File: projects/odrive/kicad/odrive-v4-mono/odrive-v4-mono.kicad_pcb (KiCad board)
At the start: 4 copper layers, 140 x 112 mm, 325 parts, among them J1 PC 16/2-ST, J10 ENC_M1_JST-GH, J11 ENC_SPI_JST-GH, J12 GPIO_2x4, J13 BRAKE_EXT, J2 M0 A/B/C, J4 FTSH-105-01-L-DV-K, J5 FAN 12V 150mA MAX, J6 USB4105-GF-A, J7 JST-GH-4 CAN, J8 JST-GH-4 CAN, J9 ENC_M0_JST-GH, Q1 NVMFS5C628NL | BSC027N10NS5, Q10 NVMFS5C628NL, Q11 NVMFS5C628NL, Q12 NVMFS5C628NL, Q13 NVMFS5C628NL, Q14 NVMFS5C628NL, Q15 NVMFS5C628NL, Q16 NVMFS5C628NL, Q17 NVMFS5C628NL, Q18 NVMFS5C628NL, Q19 NVMFS5C628NL, Q20 NVMFS5C628NL, Q21 NVMFS5C628NL, Q50 NVMFS5C628NL/BSC027N10NS5, Q51 NVMFS5C628NL/BSC027N10NS5, SW1 CAN_TERM, U10 TLV9062, U11 TMUX1204, U12 TLV7031, U13 TLV431, U14 74LVC1G04, U15 74LVC1G08, U16 TPD4E05U06, U2 STM32F405RGT6, U20 LM5164DDA, U21 LMR51430, U22 TLV75533PDBV, U23 TPS7A2033DBV, U25 74LVC1G06, U26 TLV7031DBV, U27 74LVC1G08, U28 TPS3840DL30, U3 DRV8353RS, U30 TPS2553DBV, U31 TPS2553DBV, U32 TPS2553DBV, U33 USBLC6-2SC6, U34 TCAN1042HGV, U35 SN74LVC2G17, U36 SN74LVC2G17, U37 SN74LVC2G17, U38 TPD4E05U06, U39 TPD4E05U06, U40 SN74LVC1G125, U41 TPD4E05U06, U42 TPD1E10B06, U50 UCC27517A, U51 INA181A2, U52 TLV7031, U53 74LVC1G74, U54 74LVC1G32, U55 74LVC1G08, Y1 8MHz

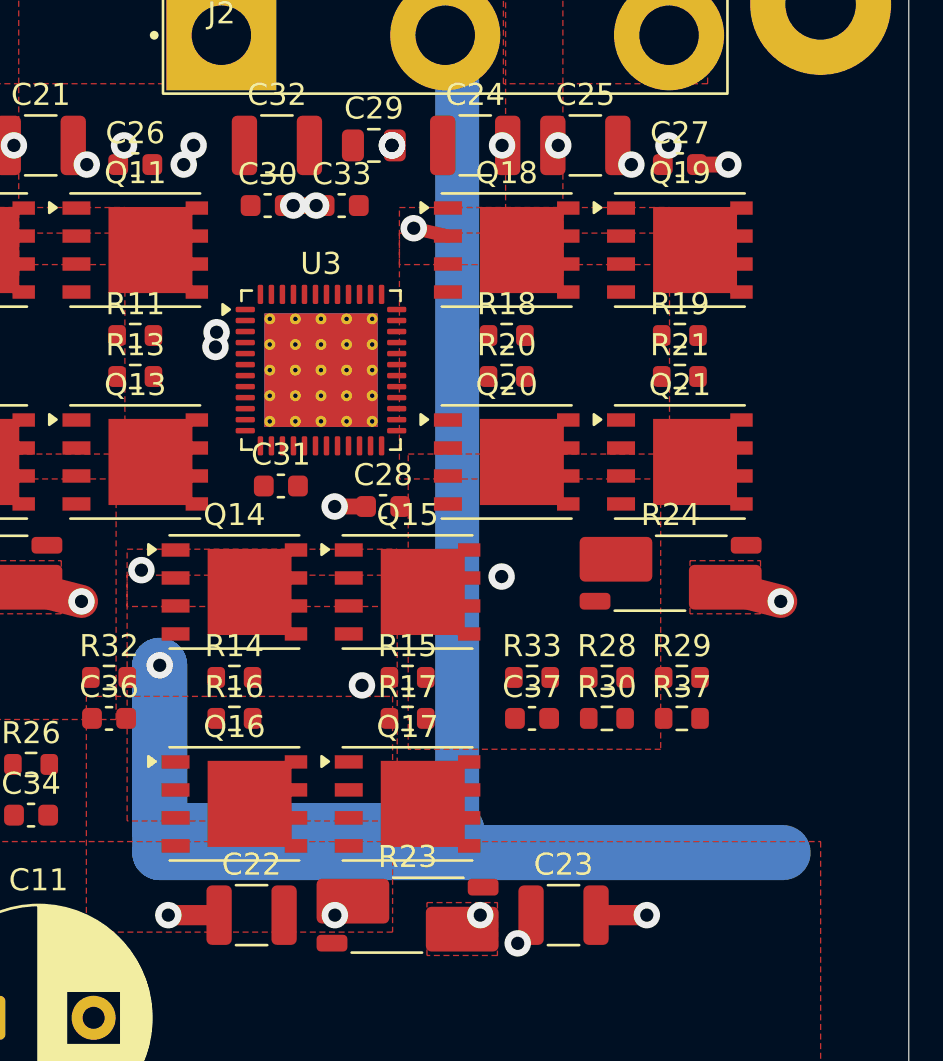
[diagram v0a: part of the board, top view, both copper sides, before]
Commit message: Phase 0 closed: power frozen - 79 items locked, DRC zero, evaluator floors met
The lock is the load-bearing step: ImportSpecctraSES deletes every
unlocked track and via board-wide, so nothing autorouted can be imported
until the power copper is untouchable. All 78 tracks/vias locked via the
SWIG script from the strategy (verified working on 10.0.4), plus the
re-created second M0_B corridor via, 79 total, every one carrying
'(locked yes)' in the file.

Cleanup en route: the dangling leftovers found by the warning-level DRC
sweep - one 28mm orphan segment and a stray SRC_B via from the old B
corridor, plus the mystery M0_CPL via, which turned out to be my own
bug: an earlier via-clone found no '(at 156.0 84.0)' match because KiCad
normalizes '156.0' to '156' on save, and the fallback rfind cloned the
last via in the file instead - a silent exact-duplicate. Coordinate
patterns against a saved board must use the normalized form.

Rule areas are formally skipped, documented in the strategy: KiCad
keepouts cannot exempt existing items and the power columns are full of
our own stitch copper. Locks + layer confinement + G3/G4 gates carry
that protection instead.

Gate results: kicad-cli DRC 0 errors; power_eval via floors all met
(DCBUS 23, PGND 22, M0_B 2); the 43 remaining power unconnected are the
known thin-trace pile (driver pins, bootstrap, snubber taps, brake tail)
owned by the Phase-1 escape pass. Next: escape pre-pass for U2/U3,
route_eval.py, then the freerouting-vs-KRT tournament.
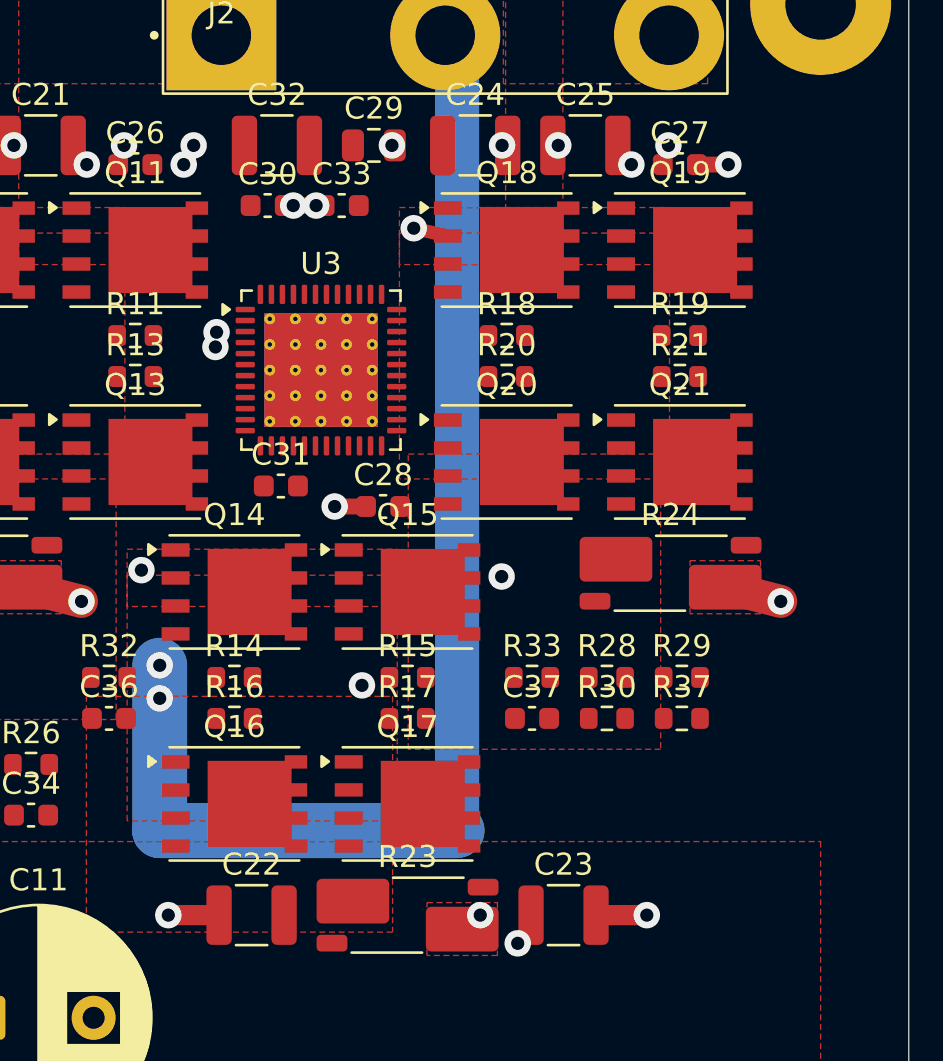
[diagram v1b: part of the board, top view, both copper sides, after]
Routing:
- net /MotorCell M0/M0_B: track 94.0 -> 57.2 mm, vias 1 -> 2
- net /MotorCell M0/M0_SRC_B: vias 1 -> 0
- net /MotorCell M0/M0_CPL: vias 2 -> 1

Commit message: Phase 1: escape pre-pass for the two pin funnels - 87 stubs, DRC zero
The board's routing difficulty concentrates at U2 (LQFP-64, 55 signal
pins) and U3 (QFN-48, 42): inter-pin capacity at 0.5mm pitch with our
rules is exactly zero, so every pin must be walked out of the pad field
before any global routing. This pass does it deterministically.

v1 (radial fan from package centre) taught the lesson: corner pins'
diagonal exits cut toward neighbouring pads - 70 clearance violations at
0.13-0.19mm - because a TRACK has no Reference and the intra-footprint
DRU rule cannot bless it; and the circle approximation of elongated QFN
pads in the self-checker rejected all 97 pins first (the pad's long axis
points ALONG the stub; the lateral half-width is the short dim).

v2: perpendicular exit from each package side, lane-centred by
construction (0.225mm to each neighbour pad against the 0.2 rule),
seg-to-rect distances in the self-check, NC pins excluded, no via rows
(the 39 crossing pins keep plain ring stubs; the router vias beyond the
ring where there is room). 87 of 89 pins stubbed; the 2 drops are U3's
bootstrap pins whose caps sit directly in front - a short manual tap.

Result: kicad-cli DRC 0 errors, 84mm of signal copper on 79 nets,
congestion peak 8 (the rings), corner cost unchanged. Escape stubs are
deliberately UNLOCKED for now - they must be locked at Phase-2 entry
before any SES import, alongside the power copper.
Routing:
- net nFAULT: track 0.00 -> 2.00 mm
- net SPI3_SCK: track 0.00 -> 2.00 mm
- net SPI3_MOSI: track 0.00 -> 2.00 mm
- net SPI3_MISO: track 0.00 -> 2.00 mm
- net M0_nCS: track 0.00 -> 2.00 mm
- net M0_CL: track 0.00 -> 2.00 mm
- net M0_CH: track 0.00 -> 2.00 mm
- net M0_BL: track 0.00 -> 2.00 mm
- net M0_BH: track 0.00 -> 2.00 mm
- net M0_AL: track 0.00 -> 2.00 mm
- net M0_AH: track 0.00 -> 2.00 mm
- net VBUS_S: track 0.00 -> 1.00 mm
- net USB_DP: track 0.00 -> 1.00 mm
- net USB_DM: track 0.00 -> 1.00 mm
- net NRST: track 0.00 -> 1.00 mm
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
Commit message: Build the ground bridge: NT2 moved to the split, planes now tied in copper
The user's question 'is the separation gap correct?' surfaced two real
findings. Measured: the In1 gap is a clean 2.00mm (PGND fill to y=112.00,
GND from y=114.00, no accidental bridges) - but NT2, the PGND-GND net
tie, sat at (91,134) deep in the logic half with its PGND pad connected
to nothing: the two ground domains were tied on the schematic and
genuinely isolated in copper. And the tie's location was wrong for the
17 signals that cross the split (spread x=90..163, median ~121, the
dense driver trunk at 155-163): return currents want the stitch point
where the signals cross.

Fixed now rather than later because placement is free today and
expensive after the autorouter: NT2 moved to (139,120) hard against the
split at the crossing corridor - the x chosen by scanning 120..140 for
a vertical lane clear of every pad and via, which exists only at 139.
The bridge is two 0.5mm stubs from the tie pads to two 1.2/0.6 vias,
one into each plane, all four locked. First attempt used 1.0mm stubs
whose edges met exactly at y=120 between the 1mm-spaced tie pads - a
PGND-GND short OUTSIDE the net-tie's blessed copper; pad-width stubs
fix it, and the tie carries reference current, not power.

kicad-cli DRC: 0 errors. The star point now exists physically, sits
where the crossings are, and survives the SES round trip.
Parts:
- moved NT2 50.0 mm to (139.0, 120.0), turned to 90 degrees
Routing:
- net PGND: track 29.4 -> 38.4 mm, vias 22 -> 23
- net GND: track 0.00 -> 2.00 mm, vias 0 -> 1
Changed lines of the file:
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@@
 	(footprint "NetTie:NetTie-2_SMD_Pad0.5mm"
 		(layer "F.Cu")
-		(at 91 134)
+		(at 139 120 90)
 		(property "Reference" "NT2"
 			(at 0 -1.2 0)
@@
 	)
 	(segment
+		(start 139 120.5)
+		(end 139 122.5)
+		(width 0.5)
+		(locked yes)
+		(layer "F.Cu")
+		(net "GND")
+	)
+	(via
+		(at 139 122.5)
+		(size 1.2)
+		(drill 0.6)
+		(layers "F.Cu" "B.Cu")
+		(locked yes)
+		(net "GND")
+	)
+	(segment
 		(start 159.882 70.85)
 		(end 158.882 70.85)
@@
 	)
 	(segment
+		(start 139 119.5)
+		(end 139 110.5)
+		(width 0.5)
+		(locked yes)
+		(layer "F.Cu")
+		(net "PGND")
+	)
+	(segment
 		(start 83.6 90)
 		(end 81 91.1)
@@
 		(size 1.2)
 		(drill 0.6)
+		(layers "F.Cu" "B.Cu")
+		(locked yes)
+		(net "PGND")
+	)
+	(via
+		(at 139 110.5)
+		(size 1.2)
+		(drill 0.6)
